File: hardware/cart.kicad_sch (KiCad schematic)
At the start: 9 parts, among them J2 debug-power, P1 edge connector, U1 74LVC138, U2 1.5A @ 3.3V

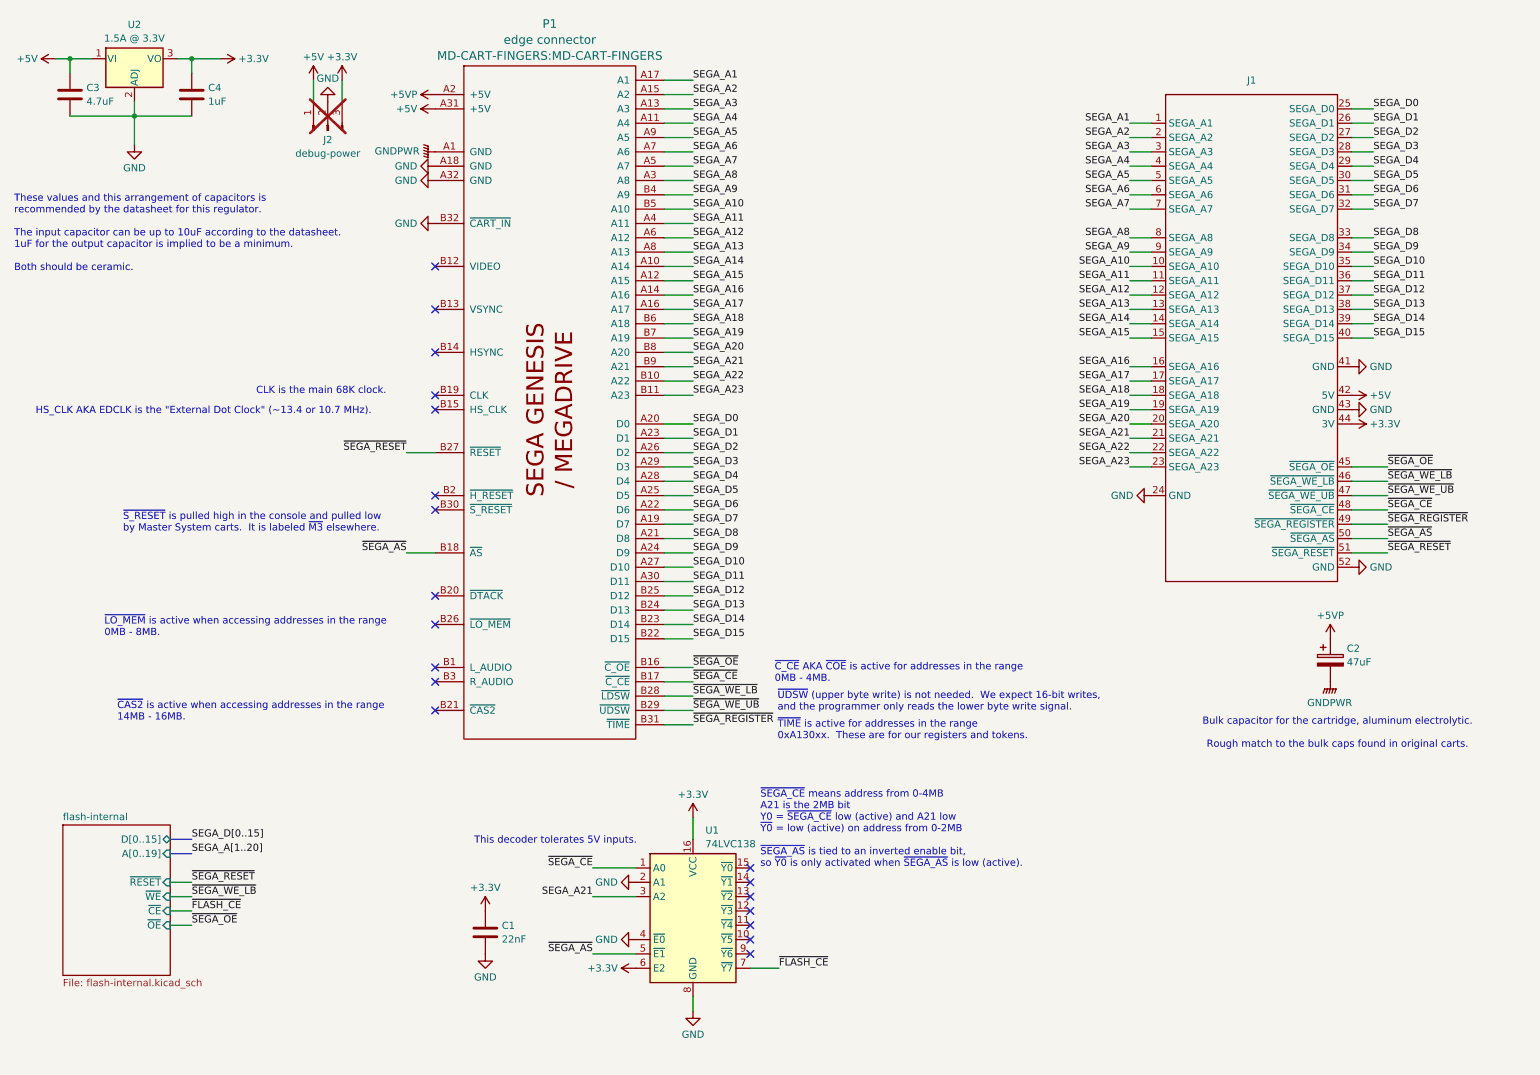
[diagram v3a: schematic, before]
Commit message: Fix cartridge board mistakes from v0.0.2
After getting the v0.0.2 cart board assembled, I found and fixed
several issues:
 - Fix address decoder output (Y0, not Y7)
 - Fix level-shifter direction for data (was backwards before)
 - Fix debug pad access to signals (level-shifters should use the
   internal signal, not the external one)
 - Avoid traces too close to the debug pads, since they can be cut
   accidentally

Also:
 - Add additional debug pad for both raw and level-shifted signals
 - Add debug pad and pin header for measuring current consumption
 - Replace bulk capacitor with SMD version
 - Remove pin headers that I didn't find all that useful in the last
   revision
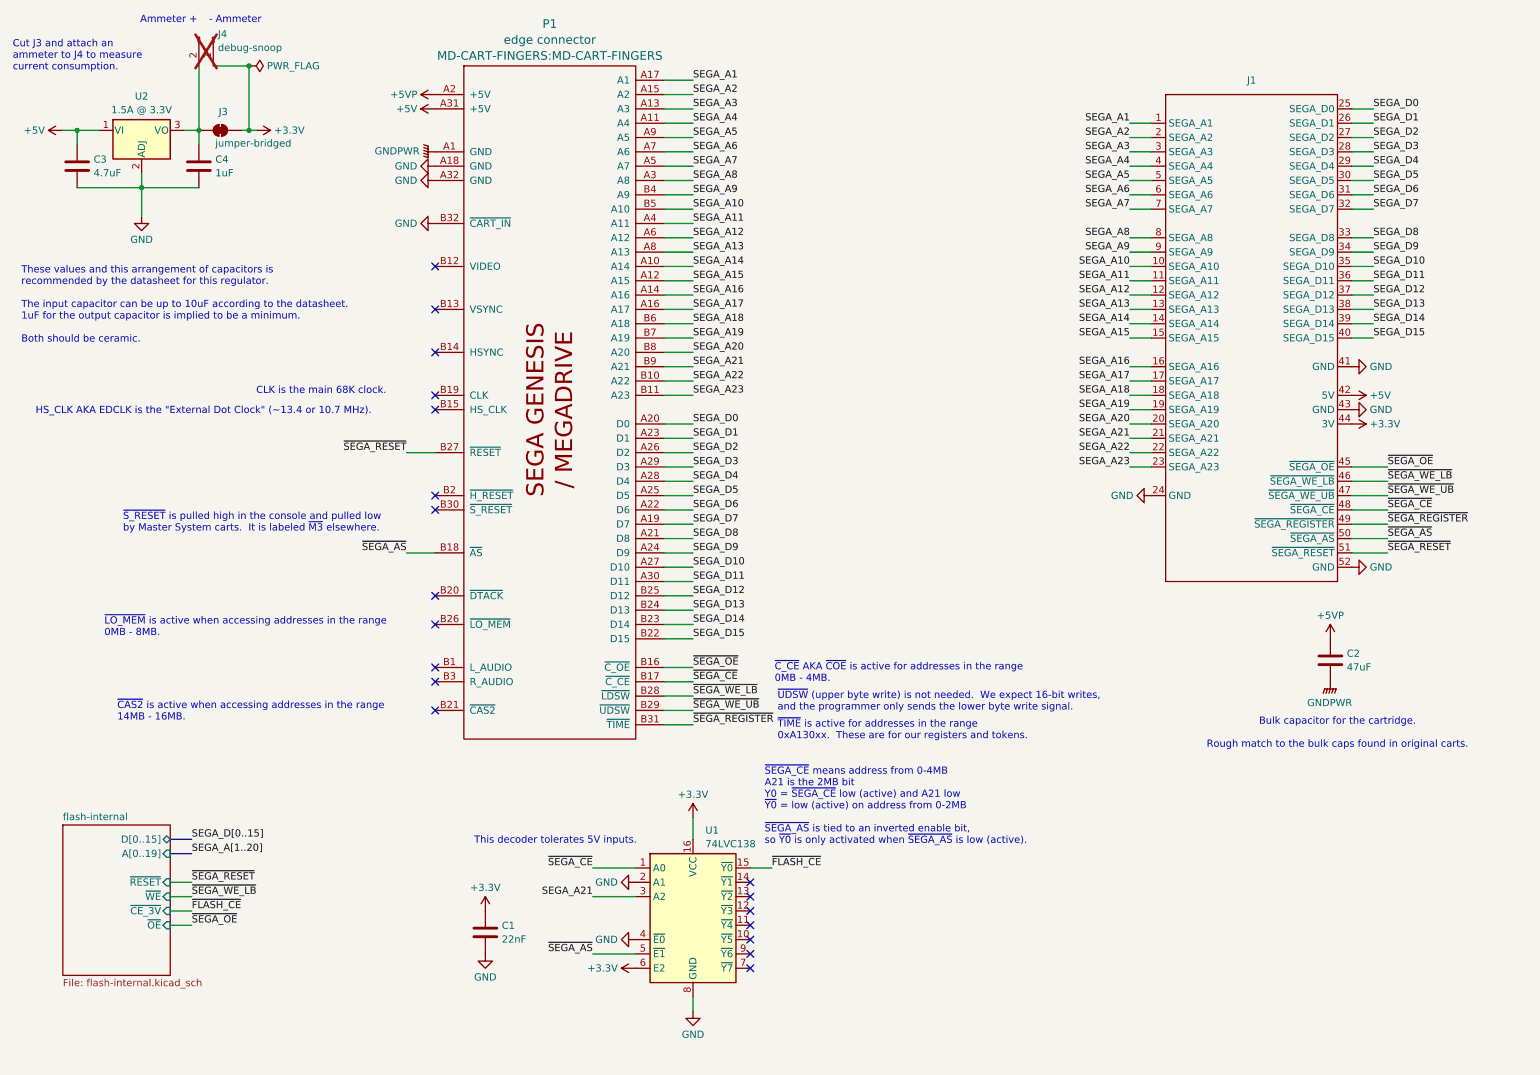
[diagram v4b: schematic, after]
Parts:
- removed J2: debug-power, Connector_PinHeader_2.54mm:PinHeader_1x03_P2.54mm_Horizontal, symbol Connector:Conn_01x03_Pin
- added J3: jumper-bridged, Jumper:SolderJumper-2_P1.3mm_Bridged_Pad1.0x1.5mm, symbol Jumper:SolderJumper_2_Bridged
- added J4: debug-snoop, Connector_PinHeader_2.54mm:PinHeader_1x02_P2.54mm_Horizontal, symbol Connector:Conn_01x02_Pin
- C2: footprint Capacitor_THT:CP_Radial_D5.0mm_P2.00mm -> Capacitor_SMD:C_1206_3216Metric; symbol Device:C_Polarized -> Device:C; JLCPCB Part Number (none) -> C96123; Mouser Part Number 710-860010372004 -> 187-CL31A476MPHNNNE; Part Number 860010372004 -> CL31A476MPHNNNE
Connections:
- net +3.3V: now also J3.2 (B), J4.1 (Pin_1); no longer C4.1, U2.3 (VO)
- net ~{FLASH_CE}: now also U1.15 (~{Y0}); no longer U1.7 (~{Y7})
- new net: C4.1, J3.1 (A), J4.2 (Pin_2), U2.3 (VO)
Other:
- sheet flash-internal ports: added ~{CE_3V}; removed ~{CE}
- note added: "- Ammeter"
- note added: "Ammeter +"
- note added: "Bulk capacitor for the cartridge. Rough match to the bulk caps found in original carts."
- note added: "Cut J3 and attach an ammeter to J4 to measure current consumption."
- note added: "~{UDSW} (upper byte write) is not needed. We expect 16-bit writes, and the programmer only sends the lower byte write signal."
- note removed: "Bulk capacitor for the cartridge, aluminum electrolytic. Rough match to the bulk caps found in original carts."
- note removed: "~{UDSW} (upper byte write) is not needed. We expect 16-bit writes, and the programmer only reads the lower byte write signal."
- moved on the sheet: C3, C4, U2

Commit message: Streamline cart board
 - Let JLCPCB populate the base header
 - Switch regulator for SMD version that JLCPCB can populate
 - Move components for easier routing, easier access to ammeter header
 - Add explanatory text in the silkscreen for each section of the PCB
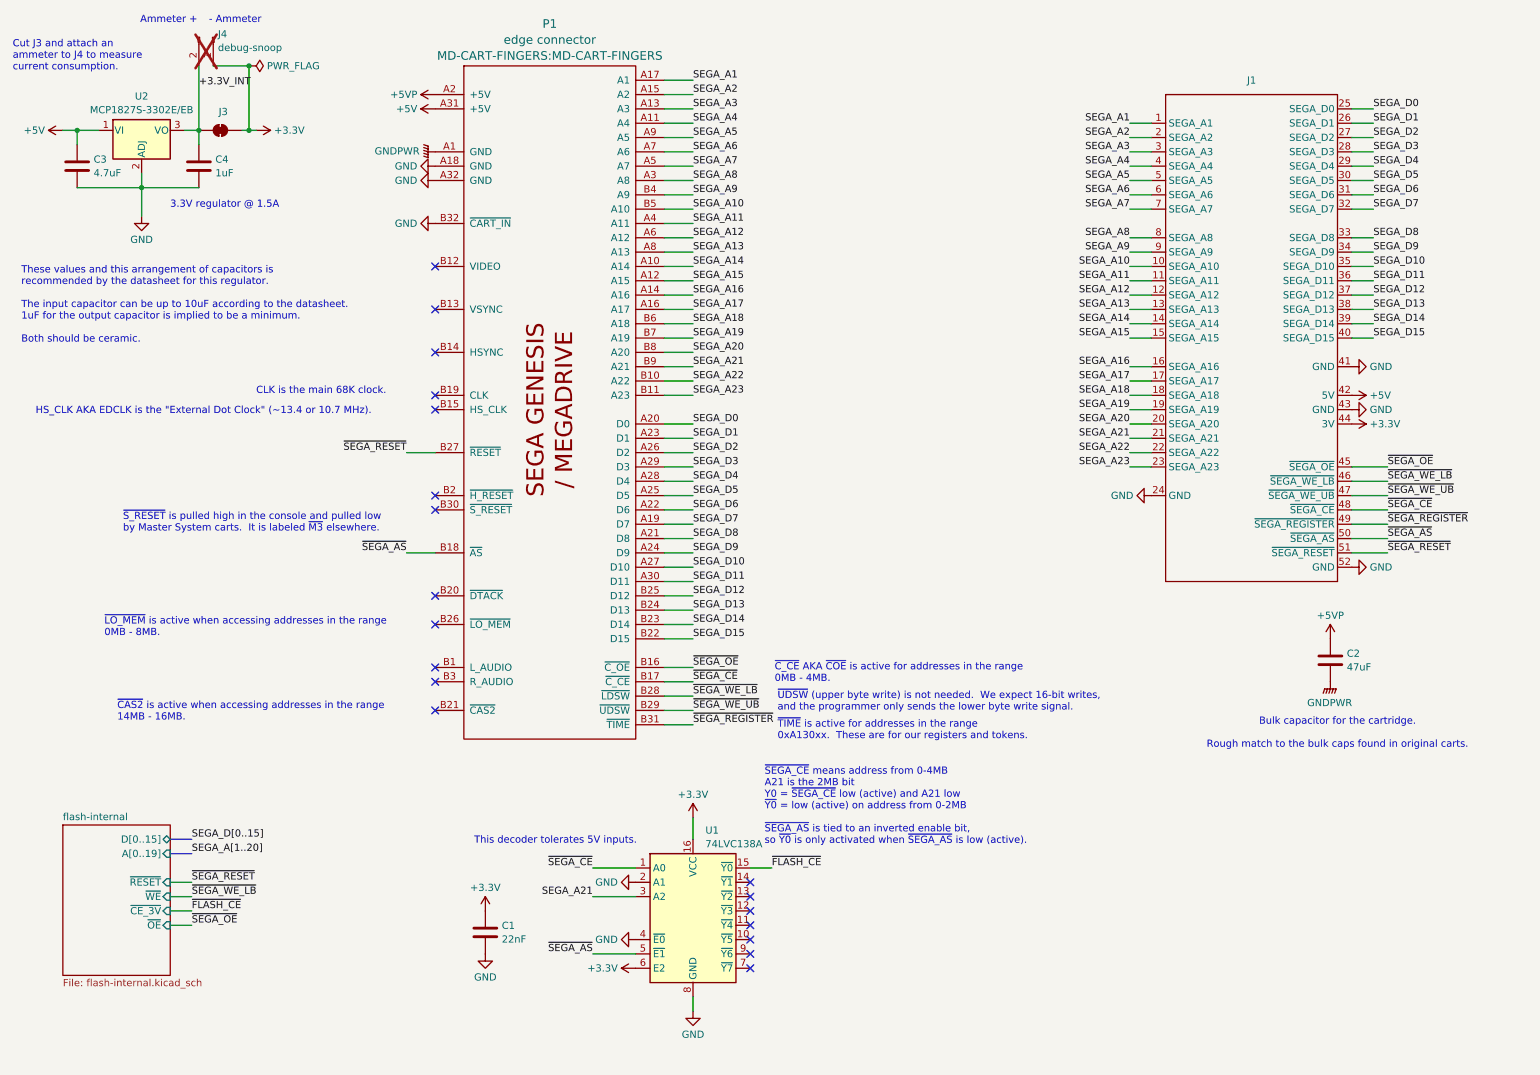
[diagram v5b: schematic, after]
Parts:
- J1: JLCPCB Part Number (none) -> C2883999; Mouser Part Number (none) -> 200-CES12601TD; Part Number (none) -> X6521FV-2x26-C85D32
- J3: value jumper-bridged -> ~
- U1: value 74LVC138 -> 74LVC138A
- U2: value 1.5A @ 3.3V -> MCP1827S-3302E/EB; footprint Package_TO_SOT_THT:TO-220-3_Horizontal_TabDown -> Package_TO_SOT_SMD:TO-252-3_TabPin2; JLCPCB Part Number C641199 -> C641200; Mouser Part Number 579-MCP1827S3302E/AB -> 579-MCP1827S3302E/EB; Part Number MCP1827S-3302E/AB -> MCP1827S-3302E/EB
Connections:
- net +3.3V_INT: now reaches C4.1, J3.1 (A), J4.2 (Pin_2), U2.3 (VO)
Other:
- note added: "3.3V regulator @ 1.5A"
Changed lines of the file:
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@@
 		)
 	)
+	(text "3.3V regulator @ 1.5A"
+		(exclude_from_sim no)
+		(at 50.292 46.228 0)
+		(effects
+			(font
+				(size 1.27 1.27)
+			)
+		)
+	)
 	(text "~{TIME} is active for addresses in the range\n0xA130xx.  These are for our registers and tokens."
 		(exclude_from_sim no)
@@
 		)
 	)
+	(label "+3.3V_INT"
+		(at 45.72 25.3471 0)
+		(fields_autoplaced yes)
+		(effects
+			(font
+				(size 1.27 1.27)
+			)
+			(justify left bottom)
+		)
+	)
 	(label "SEGA_A3"
 		(at 210.82 36.83 180)
@@
 			)
 		)
-		(property "JLCPCB Part Number" ""
+		(property "JLCPCB Part Number" "C2883999"
 			(at 232.41 26.67 0)
 			(effects
@@
 			)
 		)
-		(property "Mouser Part Number" ""
+		(property "Mouser Part Number" "200-CES12601TD"
 			(at 232.41 26.67 0)
 			(effects
@@
 			)
 		)
-		(property "Part Number" ""
+		(property "Part Number" "X6521FV-2x26-C85D32"
 			(at 232.41 26.67 0)
 			(effects
@@
 			)
 		)
-		(property "Value" "1.5A @ 3.3V"
+		(property "Value" "MCP1827S-3302E/EB"
 			(at 35.56 29.3948 0)
 			(effects
@@
 			)
 		)
-		(property "Footprint" "Package_TO_SOT_THT:TO-220-3_Horizontal_TabDown"
+		(property "Footprint" "Package_TO_SOT_SMD:TO-252-3_TabPin2"
 			(at 35.56 27.305 0)
 			(effects
@@
 			)
 		)
-		(property "Mouser Part Number" "579-MCP1827S3302E/AB"
+		(property "Mouser Part Number" "579-MCP1827S3302E/EB"
 			(at 35.56 33.02 0)
 			(effects
@@
 			)
 		)
-		(property "Part Number" "MCP1827S-3302E/AB"
+		(property "Part Number" "MCP1827S-3302E/EB"
 			(at 35.56 33.02 0)
 			(effects
@@
 			)
 		)
-		(property "JLCPCB Part Number" "C641199"
+		(property "JLCPCB Part Number" "C641200"
 			(at 35.56 33.02 0)
 			(effects
@@
 			)
 		)
-		(property "Value" "74LVC138"
+		(property "Value" "74LVC138A"
 			(at 135.5441 159.5698 0)
 			(effects
@@
 			)
 		)
-		(property "Value" "jumper-bridged"
+		(property "Value" "~"
 			(at 55.372 35.306 0)
 			(effects

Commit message: Correct cart board titles
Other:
- title: Kinetoscope Cartridge Connector -> Kinetoscope Cartridge & Flash Board
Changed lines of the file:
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@@
 	(paper "A4")
 	(title_block
-		(title "Kinetoscope Cartridge Connector")
+		(title "Kinetoscope Cartridge & Flash Board")
 	)
 	(junction
